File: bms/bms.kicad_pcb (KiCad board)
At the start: 2 copper layers, 87.2 x 145.7 mm, 35 parts, among them J10 Conn_02x10_Odd_Even, J11 Conn_02x08_Odd_Even, J12 Conn_02x10_Odd_Even, J13 Conn_02x08_Odd_Even, J14 Conn_02x08_Odd_Even, J15 Conn_02x10_Odd_Even, J2 Conn_01x08_Socket, J3 Conn_01x06_Socket, J5 Conn_01x10_Socket, J6 Conn_01x08_Socket

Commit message: PCB modified - lange update
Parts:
- added C1: 1uF, Capacitor_SMD:C_0805_2012Metric_Pad1.18x1.45mm_HandSolder, F.Cu at (59.6, 59.8)
- added C2: 2.2uF, Capacitor_SMD:C_0805_2012Metric_Pad1.18x1.45mm_HandSolder, F.Cu at (60.7, 71.5)
- added U1: TLV76150DCY, Package_TO_SOT_SMD:SOT-223-3_TabPin2, F.Cu at (59.6, 65.5)
- D1: footprint Diode_SMD:D_SMB -> Diode_THT:D_A-405_P7.62mm_Horizontal
- moved Soft_G_B1-2 78.7 mm to (127.1, 91.4), turned to 90 degrees
- moved Soft_G_B3-4 73.9 mm to (127.1, 100.4), turned to 90 degrees
- moved Soft_G_B5-6 71.2 mm to (127.1, 109.4), turned to 90 degrees
- moved Soft_G_B7-8 70.6 mm to (127.1, 118.3), turned to 90 degrees
- moved Soft_G_B15-16 56.1 mm to (127.0, 167.7), turned to 90 degrees
- moved Soft_G_B13-14 44.8 mm to (127.0, 158.7), turned to 90 degrees
- moved Soft_G_B11-12 34.6 mm to (127.0, 149.8), turned to 90 degrees
- moved CAN_Bus_VCU1 29.4 mm to (53.8, 37.9), turned to -90 degrees
- moved Soft_G_B9-10 26.5 mm to (127.0, 140.8), turned to 90 degrees
- moved B1 14.7 mm to (50.7, 50.6)
- moved D1 14.3 mm to (56.2, 50.7), turned to 0 degrees
- moved H1 10.9 mm to (130.9, 29.1)
- moved H3 10.9 mm to (51.3, 29.1)
- moved Vdd1 4.53 mm to (58.9, 88.7)
- moved CAN_k312 0.32 mm to (80.8, 77.9)
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- renumbered Battery1 to B1, J5 to J3, J2 to J4, J6 to J5, J3 to J6
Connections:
- B1 pad 1: GND -> BAT+
- B1 pad 2: BAT+ -> GND
- J10 pad 10: unconnected-(J10-Pin_10-Pad10) -> G6
- J10 pad 12: unconnected-(J10-Pin_12-Pad12) -> G5
- J10 pad 14: unconnected-(J10-Pin_14-Pad14) -> G4
- J10 pad 16: unconnected-(J10-Pin_16-Pad16) -> G3
- J10 pad 18: unconnected-(J10-Pin_18-Pad18) -> G2
- J10 pad 20: unconnected-(J10-Pin_20-Pad20) -> G1
- J10 pad 6: unconnected-(J10-Pin_6-Pad6) -> G8
- J10 pad 8: unconnected-(J10-Pin_8-Pad8) -> G7
- J12 pad 14: unconnected-(J12-Pin_14-Pad14) -> G12
- J12 pad 16: unconnected-(J12-Pin_16-Pad16) -> G11
- J12 pad 18: unconnected-(J12-Pin_18-Pad18) -> G10
- J12 pad 2: unconnected-(J12-Pin_2-Pad2) -> G16
- J12 pad 20: unconnected-(J12-Pin_20-Pad20) -> G9
- J12 pad 4: unconnected-(J12-Pin_4-Pad4) -> G15
- J12 pad 6: unconnected-(J12-Pin_6-Pad6) -> G14
- J12 pad 8: unconnected-(J12-Pin_8-Pad8) -> G13
- J13 pad 10: G5 -> unconnected-(J13-Pin_10-Pad10)
- J13 pad 12: G6 -> unconnected-(J13-Pin_12-Pad12)
- J13 pad 14: G7 -> unconnected-(J13-Pin_14-Pad14)
- J13 pad 16: G8 -> unconnected-(J13-Pin_16-Pad16)
- J13 pad 2: G1 -> unconnected-(J13-Pin_2-Pad2)
- J13 pad 4: G2 -> unconnected-(J13-Pin_4-Pad4)
- J13 pad 6: G3 -> unconnected-(J13-Pin_6-Pad6)
- J13 pad 8: G4 -> unconnected-(J13-Pin_8-Pad8)
- J13 pad 9: Vdd -> unconnected-(J13-Pin_9-Pad9)
- J14 pad 10: G13 -> unconnected-(J14-Pin_10-Pad10)
- J14 pad 12: G14 -> unconnected-(J14-Pin_12-Pad12)
- J14 pad 14: G15 -> unconnected-(J14-Pin_14-Pad14)
- J14 pad 16: G16 -> unconnected-(J14-Pin_16-Pad16)
- J14 pad 2: G9 -> unconnected-(J14-Pin_2-Pad2)
- J14 pad 4: G10 -> unconnected-(J14-Pin_4-Pad4)
- J14 pad 6: G11 -> unconnected-(J14-Pin_6-Pad6)
- J14 pad 8: G12 -> unconnected-(J14-Pin_8-Pad8)
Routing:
- net Vdd: track 107.1 -> 138.3 mm
- net GND: track 0.00 -> 29.1 mm, vias 0 -> 1
- net BAT+: track 44.3 -> 70.8 mm
- net CAN_H_k: track 36.5 -> 58.4 mm
- net CAN_L_k: track 36.6 -> 57.7 mm
- net G8: track 0.45 -> 16.0 mm
- net G7: track 0.54 -> 16.0 mm
- net G6: track 0.00 -> 14.4 mm
- net G5: track 0.09 -> 14.4 mm
- net G16: track 0.00 -> 13.7 mm
- net G15: track 0.05 -> 13.7 mm
- net G3: track 0.00 -> 12.8 mm
- net G4: track 0.00 -> 12.8 mm
- net G11: track 0.00 -> 12.6 mm
- net G12: track 0.00 -> 12.6 mm
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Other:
- board size 87.2 x 145.7 mm -> 87.2 x 156.6 mm

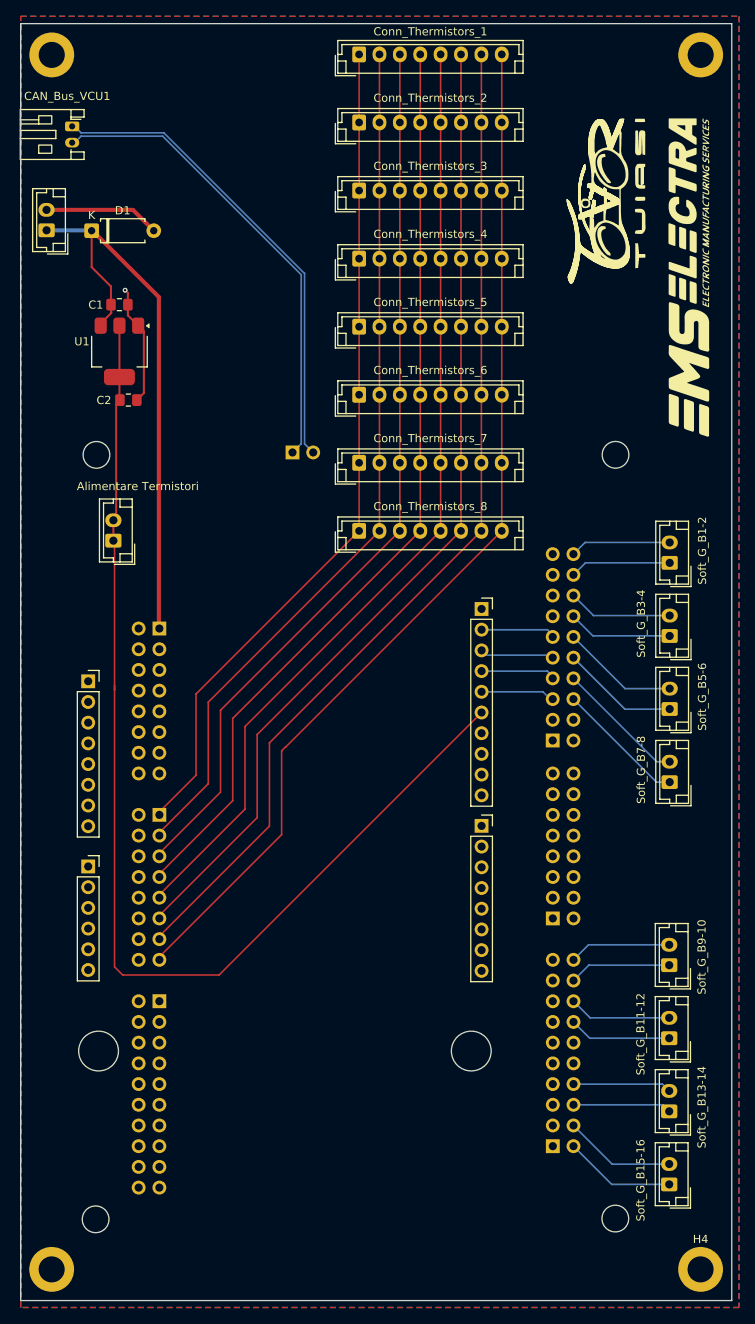
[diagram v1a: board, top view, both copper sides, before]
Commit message: 1x GND plane now removed
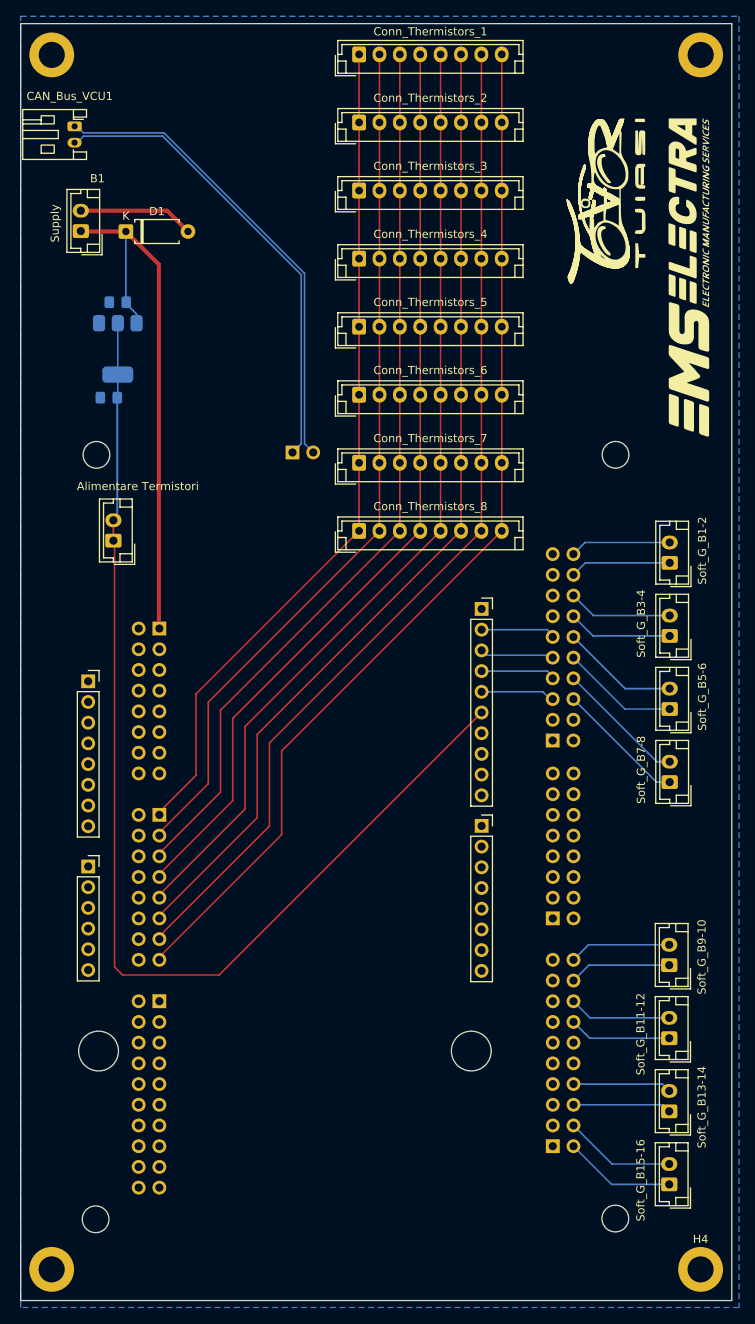
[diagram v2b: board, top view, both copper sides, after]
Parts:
- B1: value Conn_01x02_Pin -> Supply
- C1, C2, U1: moved to B.Cu
- moved D1 4.20 mm to (60.4, 50.8)
- moved B1 4.20 mm to (54.9, 50.7)
- moved C2 2.42 mm to (58.3, 71.2), turned to 180 degrees
- moved C1 0.36 mm to (59.4, 59.5), turned to 180 degrees
- moved U1 0.36 mm to (59.4, 65.2)
- moved CAN_Bus_VCU1 0.30 mm to (54.1, 37.9)
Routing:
- net GND: track 29.1 -> 14.3 mm, vias 1 -> 0
- net BAT+: track 70.8 -> 67.6 mm
- removed copper zone on F.Cu, net GND

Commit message: CAN_IN & CAN_OUT - added
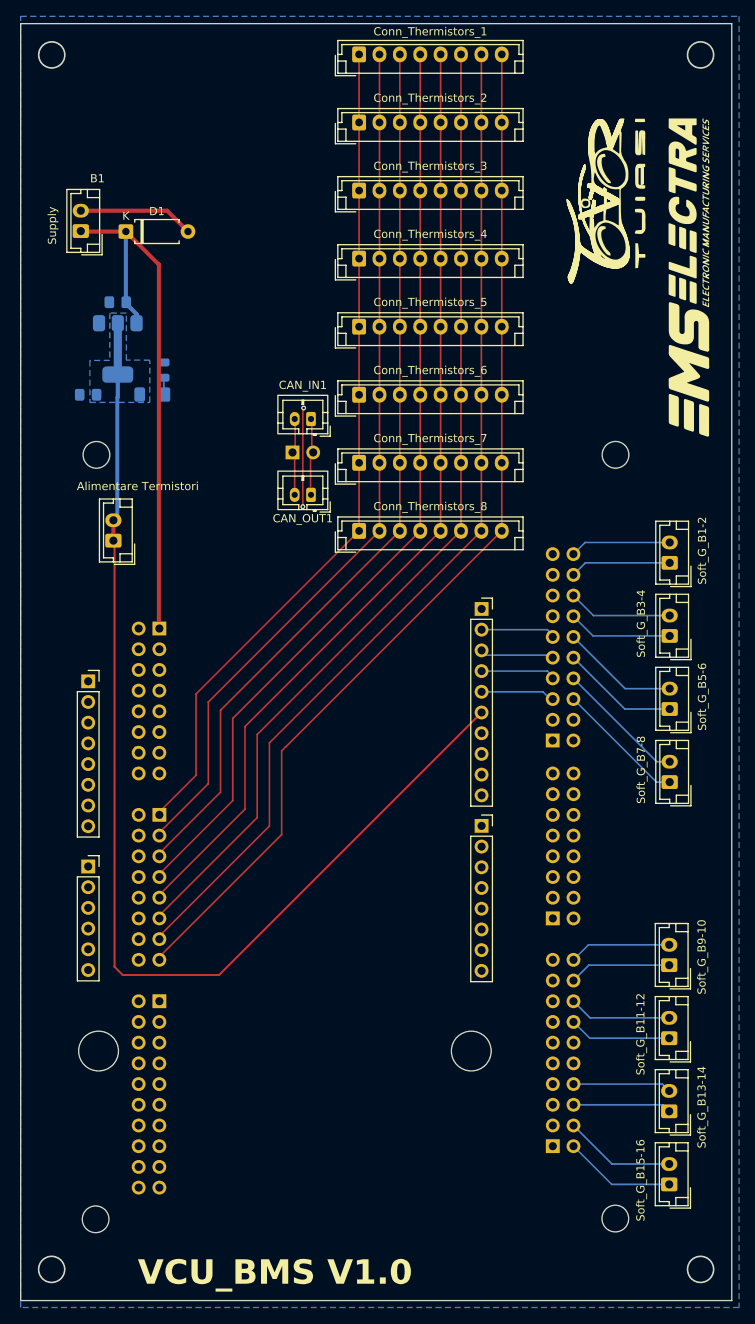
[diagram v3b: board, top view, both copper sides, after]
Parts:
- removed CAN_Bus_VCU1: Conn_01x02_Pin, Connector_JST:JST_PH_S2B-PH-K_1x02_P2.00mm_Horizontal
- removed H1, H2, H3, H4: MountingHole_Pad, MountingHole:MountingHole_3.2mm_M3_ISO14580_Pad
- added CAN_IN1: Conn_01x02_Pin, Connector_JST:JST_PH_B2B-PH-K_1x02_P2.00mm_Vertical, F.Cu at (83.1, 73.8)
- added CAN_OUT1: Conn_01x02_Pin, Connector_JST:JST_PH_B2B-PH-K_1x02_P2.00mm_Vertical, F.Cu at (83.1, 83.1)
- added D14: LED, LED_SMD:LED_0805_2012Metric, B.Cu at (65.0, 67.8)
- added R54: 1k, Resistor_SMD:R_1206_3216Metric_Pad1.30x1.75mm_HandSolder, B.Cu at (63.6, 70.8)
- moved C2 2.56 mm to (55.8, 70.8)
- renumbered Vdd1 to 5Vdd1
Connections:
- net G1 renamed G01
- net G2 renamed G02
- net G3 renamed G03
- net G4 renamed G04
- net G5 renamed G05
- net G6 renamed G06
- net G7 renamed G07
- net G8 renamed G08
- net G9 renamed G09
- net Vdd renamed 5V1
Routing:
- net CAN_H_k: track 58.1 -> 9.76 mm
- net CAN_L_k: track 57.4 -> 9.76 mm
- net GND: track 14.3 -> 26.4 mm, vias 0 -> 2
- net Net-(D14-A): track 0.00 -> 2.13 mm
- added copper zone on B.Cu, net 5V1
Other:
- outline, holes or cut-outs redrawn
- board text added: "5V"
- board text added: "VCU_BMS V1.0"

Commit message: Moved components on front size for better ground plane
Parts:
- C1, C2, D14, R54, U1: moved to F.Cu
- moved C2 9.83 mm to (65.6, 70.8), turned to 0 degrees
- moved D14 8.73 mm to (56.3, 67.8)
- moved R54 5.93 mm to (57.7, 70.8), turned to 180 degrees
- moved C1 2.55 mm to (62.0, 59.5), turned to 0 degrees
- moved U1 2.55 mm to (62.0, 65.2)
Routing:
- net GND: track 26.4 -> 33.7 mm, vias 2 -> 5
- net BAT+: track 67.6 -> 71.8 mm
- net 5V1: track 138.0 -> 139.7 mm
- net SCK: track 8.91 -> 9.63 mm
- added copper zone on F.Cu, net 5V1
- removed copper zone on B.Cu, net 5V1

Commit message: Routed all signals over GND planes
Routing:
- net 5V1: track 139.7 -> 155.9 mm
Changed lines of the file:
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@@
 	)
 	(segment
-		(start 117.705485 100.408735)
-		(end 115.29 97.99325)
-		(width 0.2)
-		(layer "F.Cu")
-		(net "G04")
-	)
-	(segment
-		(start 127.1 100.408735)
-		(end 117.705485 100.408735)
-		(width 0.2)
-		(layer "F.Cu")
-		(net "G04")
-	)
-	(segment
-		(start 115.29 95.45325)
-		(end 117.745485 97.908735)
-		(width 0.2)
-		(layer "F.Cu")
-		(net "G03")
-	)
-	(segment
-		(start 117.745485 97.908735)
-		(end 127.1 97.908735)
-		(width 0.2)
-		(layer "F.Cu")
-		(net "G03")
-	)
-	(segment
-		(start 127.040277 158.722547)
-		(end 116.102547 158.722547)
-		(width 0.2)
-		(layer "F.Cu")
-		(net "G14")
-	)
-	(segment
-		(start 116.102547 158.722547)
-		(end 115.3 157.92)
-		(width 0.2)
-		(layer "F.Cu")
-		(net "G14")
-	)
-	(segment
-		(start 115.3 155.38)
-		(end 126.19773 155.38)
-		(width 0.2)
-		(layer "F.Cu")
-		(net "G13")
-	)
-	(segment
-		(start 126.19773 155.38)
-		(end 127.040277 156.222547)
-		(width 0.2)
-		(layer "F.Cu")
-		(net "G13")
-	)
-	(segment
-		(start 127.040277 167.686833)
-		(end 119.986833 167.686833)
-		(width 0.2)
-		(layer "F.Cu")
-		(net "G16")
-	)
-	(segment
-		(start 119.986833 167.686833)
-		(end 115.3 163)
-		(width 0.2)
-		(layer "F.Cu")
-		(net "G16")
-	)
-	(segment
-		(start 120.026833 165.186833)
-		(end 115.3 160.46)
-		(width 0.2)
-		(layer "F.Cu")
-		(net "G15")
-	)
-	(segment
-		(start 127.040277 165.186833)
-		(end 120.026833 165.186833)
-		(width 0.2)
-		(layer "F.Cu")
-		(net "G15")
-	)
-	(segment
-		(start 104.025 99.64)
-		(end 104.91825 100.53325)
-		(width 0.2)
-		(layer "F.Cu")
-		(net "CS")
-	)
-	(segment
-		(start 104.91825 100.53325)
-		(end 112.75 100.53325)
-		(width 0.2)
-		(layer "F.Cu")
-		(net "CS")
-	)
-	(segment
-		(start 104.025 102.18)
-		(end 104.91825 103.07325)
-		(width 0.2)
-		(layer "F.Cu")
-		(net "SOUT")
-	)
-	(segment
-		(start 104.91825 103.07325)
-		(end 112.75 103.07325)
-		(width 0.2)
-		(layer "F.Cu")
-		(net "SOUT")
-	)
-	(segment
-		(start 104.025 104.72)
-		(end 104.91825 105.61325)
-		(width 0.2)
-		(layer "F.Cu")
-		(net "MISO")
-	)
-	(segment
-		(start 104.91825 105.61325)
-		(end 112.75 105.61325)
-		(width 0.2)
-		(layer "F.Cu")
-		(net "MISO")
-	)
-	(segment
-		(start 111.85675 107.26)
-		(end 104.025 107.26)
-		(width 0.2)
-		(layer "F.Cu")
-		(net "SCK")
-	)
-	(segment
-		(start 112.75 108.15325)
-		(end 111.85675 107.26)
-		(width 0.2)
-		(layer "F.Cu")
-		(net "SCK")
-	)
-	(segment
-		(start 112.688375 107.851625)
-		(end 112.148375 107.851625)
-		(width 0.2)
-		(layer "B.Cu")
-		(net "SCK")
-	)
-	(segment
-		(start 60 142)
-		(end 71.825 142)
-		(width 0.25)
-		(layer "F.Cu")
-		(net "5V1")
-	)
-	(segment
-		(start 59 88.86)
-		(end 59 141)
-		(width 0.25)
-		(layer "F.Cu")
-		(net "5V1")
-	)
-	(segment
-		(start 71.825 142)
-		(end 104.025 109.8)
-		(width 0.25)
+		(start 56.311822 68.735002)
+		(end 56.311822 70.649999)
+		(width 0.2)
+		(layer "F.Cu")
+		(net "Net-(D14-A)")
+	)
+	(segment
+		(start 56.311822 70.649999)
+		(end 56.161821 70.8)
+		(width 0.2)
+		(layer "F.Cu")
+		(net "Net-(D14-A)")
+	)
+	(segment
+		(start 98.75 142.25)
+		(end 101.925 139.075)
+		(width 0.3)
+		(layer "F.Cu")
+		(net "5V1")
+	)
+	(segment
+		(start 59 141)
+		(end 60.25 142.25)
+		(width 0.3)
+		(layer "F.Cu")
+		(net "5V1")
+	)
+	(segment
+		(start 101.925 139.075)
+		(end 101.925 111.9)
+		(width 0.3)
 		(layer "F.Cu")
 		(net "5V1")
@@
 	)
 	(segment
+		(start 101.925 111.9)
+		(end 104.025 109.8)
+		(width 0.3)
+		(layer "F.Cu")
+		(net "5V1")
+	)
+	(segment
 		(start 58.86 86.22)
 		(end 58.86 88.72)
@@
 	)
 	(segment
-		(start 59 141)
-		(end 60 142)
-		(width 0.25)
-		(layer "F.Cu")
-		(net "5V1")
-	)
-	(segment
 		(start 61.951822 83.128178)
 		(end 61.951822 68.349999)
@@
 		(start 58.86 88.72)
 		(end 59 88.86)
-		(width 0.25)
+		(width 0.3)
+		(layer "F.Cu")
+		(net "5V1")
+	)
+	(segment
+		(start 60.25 142.25)
+		(end 98.75 142.25)
+		(width 0.3)
+		(layer "F.Cu")
+		(net "5V1")
+	)
+	(segment
+		(start 59 88.86)
+		(end 59 141)
+		(width 0.3)
 		(layer "F.Cu")
 		(net "5V1")
@@
 	)
 	(segment
+		(start 117.705485 100.408735)
+		(end 115.29 97.99325)
+		(width 0.2)
+		(layer "F.Cu")
+		(net "G04")
+	)
+	(segment
+		(start 127.1 100.408735)
+		(end 117.705485 100.408735)
+		(width 0.2)
+		(layer "F.Cu")
+		(net "G04")
+	)
+	(segment
+		(start 115.29 95.45325)
+		(end 117.745485 97.908735)
+		(width 0.2)
+		(layer "F.Cu")
+		(net "G03")
+	)
+	(segment
+		(start 117.745485 97.908735)
+		(end 127.1 97.908735)
+		(width 0.2)
+		(layer "F.Cu")
+		(net "G03")
+	)
+	(segment
+		(start 127.040277 158.722547)
+		(end 116.102547 158.722547)
+		(width 0.2)
+		(layer "F.Cu")
+		(net "G14")
+	)
+	(segment
+		(start 116.102547 158.722547)
+		(end 115.3 157.92)
+		(width 0.2)
+		(layer "F.Cu")
+		(net "G14")
+	)
+	(segment
+		(start 115.3 155.38)
+		(end 126.19773 155.38)
+		(width 0.2)
+		(layer "F.Cu")
+		(net "G13")
+	)
+	(segment
+		(start 126.19773 155.38)
+		(end 127.040277 156.222547)
+		(width 0.2)
+		(layer "F.Cu")
+		(net "G13")
+	)
+	(segment
+		(start 127.040277 167.686833)
+		(end 119.986833 167.686833)
+		(width 0.2)
+		(layer "F.Cu")
+		(net "G16")
+	)
+	(segment
+		(start 119.986833 167.686833)
+		(end 115.3 163)
+		(width 0.2)
+		(layer "F.Cu")
+		(net "G16")
+	)
+	(segment
+		(start 120.026833 165.186833)
+		(end 115.3 160.46)
+		(width 0.2)
+		(layer "F.Cu")
+		(net "G15")
+	)
+	(segment
+		(start 127.040277 165.186833)
+		(end 120.026833 165.186833)
+		(width 0.2)
+		(layer "F.Cu")
+		(net "G15")
+	)
+	(segment
+		(start 104.025 99.64)
+		(end 104.91825 100.53325)
+		(width 0.2)
+		(layer "F.Cu")
+		(net "CS")
+	)
+	(segment
+		(start 104.91825 100.53325)
+		(end 112.75 100.53325)
+		(width 0.2)
+		(layer "F.Cu")
+		(net "CS")
+	)
+	(segment
+		(start 104.025 102.18)
+		(end 104.91825 103.07325)
+		(width 0.2)
+		(layer "F.Cu")
+		(net "SOUT")
+	)
+	(segment
+		(start 104.91825 103.07325)
+		(end 112.75 103.07325)
+		(width 0.2)
+		(layer "F.Cu")
+		(net "SOUT")
+	)
+	(segment
+		(start 104.025 104.72)
+		(end 104.91825 105.61325)
+		(width 0.2)
+		(layer "F.Cu")
+		(net "MISO")
+	)
+	(segment
+		(start 104.91825 105.61325)
+		(end 112.75 105.61325)
+		(width 0.2)
+		(layer "F.Cu")
+		(net "MISO")
+	)
+	(segment
+		(start 111.85675 107.26)
+		(end 104.025 107.26)
+		(width 0.2)
+		(layer "F.Cu")
+		(net "SCK")
+	)
+	(segment
+		(start 112.75 108.15325)
+		(end 111.85675 107.26)
+		(width 0.2)
+		(layer "F.Cu")
+		(net "SCK")
+	)
+	(segment
+		(start 112.688375 107.851625)
+		(end 112.148375 107.851625)
+		(width 0.2)
+		(layer "B.Cu")
+		(net "SCK")
+	)
+	(segment
 		(start 127.1 91.444449)
 		(end 116.758801 91.444449)
@@
 	)
 	(segment
-		(start 56.311822 68.735002)
-		(end 56.311822 70.649999)
-		(width 0.2)
-		(layer "F.Cu")
-		(net "Net-(D14-A)")
-	)
-	(segment
-		(start 56.311822 70.649999)
-		(end 56.161821 70.8)
-		(width 0.2)
-		(layer "F.Cu")
-		(net "Net-(D14-A)")
-	)
-	(segment
